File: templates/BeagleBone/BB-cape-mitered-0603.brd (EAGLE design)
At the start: 86.4 x 54.6 mm, 14 parts, among them IC8 EEPROM-I2CSMD

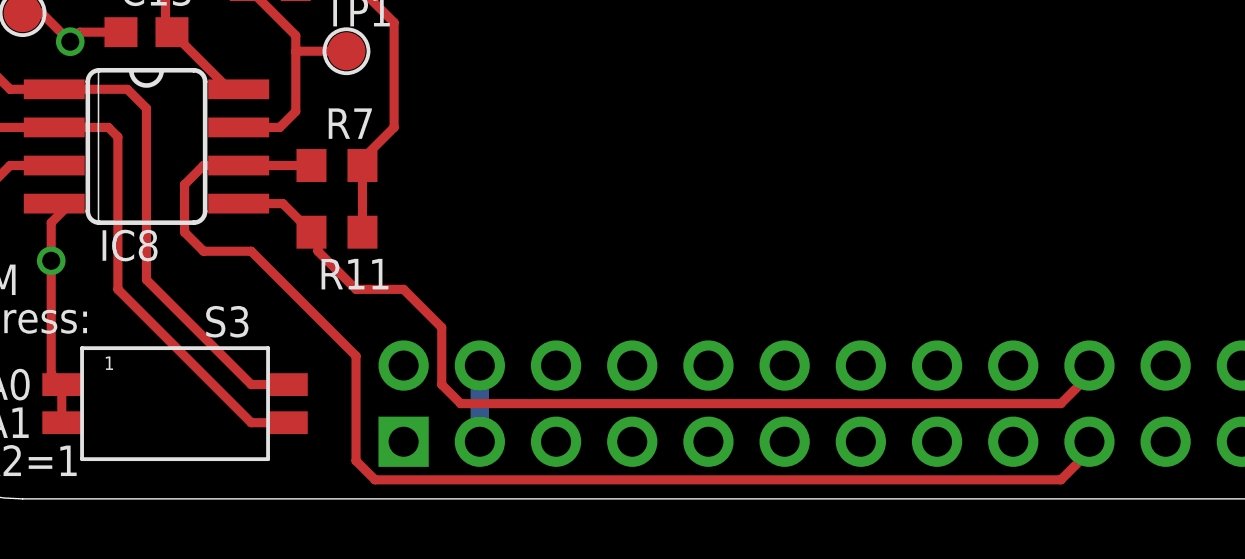
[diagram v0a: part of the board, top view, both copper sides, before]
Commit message: routed power to EEPROM
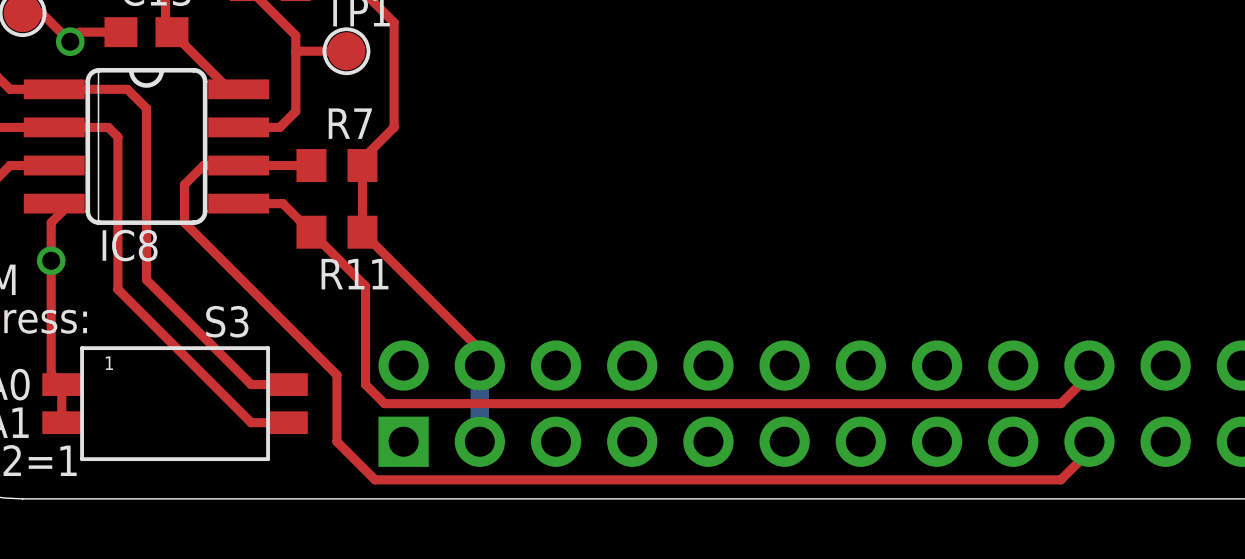
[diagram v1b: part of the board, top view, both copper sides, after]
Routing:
- net 3.3V: track 39.6 -> 45.6 mm
- net I2C2_SCL: track 42.4 -> 41.5 mm
- net I2C2_SDA: track 33.4 -> 34.0 mm
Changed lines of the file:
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@@
 <?xml version="1.0" encoding="utf-8"?>
 <!DOCTYPE eagle SYSTEM "eagle.dtd">
-<eagle version="6.3">
+<eagle version="6.4">
 <drawing>
 <settings>
@@
 <wire x1="13.5509" y1="13.6525" x2="13.2325" y2="13.6525" width="0.3048" layer="1"/>
 <wire x1="13.2325" y1="13.6525" x2="11.3275" y2="15.5575" width="0.3048" layer="1"/>
-<wire x1="17.6775" y1="8.89" x2="21.59" y2="4.445" width="0" layer="19" extent="1-1"/>
+<wire x1="21.59" y1="4.445" x2="21.59" y2="4.9775" width="0.3048" layer="1"/>
+<wire x1="21.59" y1="4.9775" x2="17.6775" y2="8.89" width="0.3048" layer="1"/>
 </signal>
 <signal name="GND">
@@
 <wire x1="15.025" y1="9.8425" x2="15.9775" y2="8.89" width="0.3048" layer="1"/>
 <wire x1="41.91" y1="4.1275" x2="40.9575" y2="3.175" width="0.3048" layer="1"/>
-<wire x1="40.9575" y1="3.175" x2="20.955" y2="3.175" width="0.3048" layer="1"/>
+<wire x1="40.9575" y1="3.175" x2="18.415" y2="3.175" width="0.3048" layer="1"/>
 <wire x1="15.875" y1="9.105" x2="15.9775" y2="8.89" width="0.3048" layer="1"/>
 <contactref element="BB1" pad="P9.20"/>
 <wire x1="41.91" y1="4.1275" x2="41.91" y2="4.445" width="0.3048" layer="1"/>
-<wire x1="20.955" y1="3.175" x2="20.32" y2="3.81" width="0.3048" layer="1"/>
-<wire x1="20.32" y1="3.81" x2="20.32" y2="5.715" width="0.3048" layer="1"/>
-<wire x1="16.1925" y1="8.255" x2="16.1925" y2="8.675" width="0.3048" layer="1"/>
-<wire x1="16.1925" y1="8.675" x2="15.9775" y2="8.89" width="0.3048" layer="1"/>
-<wire x1="20.32" y1="5.715" x2="19.05" y2="6.985" width="0.3048" layer="1"/>
-<wire x1="19.05" y1="6.985" x2="17.4625" y2="6.985" width="0.3048" layer="1"/>
-<wire x1="17.4625" y1="6.985" x2="16.1925" y2="8.255" width="0.3048" layer="1"/>
+<wire x1="18.415" y1="3.175" x2="17.78" y2="3.81" width="0.3048" layer="1"/>
+<wire x1="17.78" y1="3.81" x2="17.78" y2="7.0875" width="0.3048" layer="1"/>
+<wire x1="17.78" y1="7.0875" x2="15.9775" y2="8.89" width="0.3048" layer="1"/>
 </signal>
 <signal name="I2C2_SCL">
@@
 <contactref element="BB1" pad="P9.19"/>
 <wire x1="41.91" y1="1.905" x2="41.91" y2="1.5875" width="0.3048" layer="1"/>
-<wire x1="18.0975" y1="0.635" x2="17.4625" y2="1.27" width="0.3048" layer="1"/>
-<wire x1="11.7475" y1="10.4775" x2="11.7475" y2="8.89" width="0.3048" layer="1"/>
-<wire x1="17.4625" y1="1.27" x2="17.4625" y2="4.7625" width="0.3048" layer="1"/>
-<wire x1="17.4625" y1="4.7625" x2="13.97" y2="8.255" width="0.3048" layer="1"/>
-<wire x1="13.97" y1="8.255" x2="12.3825" y2="8.255" width="0.3048" layer="1"/>
-<wire x1="12.3825" y1="8.255" x2="11.7475" y2="8.89" width="0.3048" layer="1"/>
+<wire x1="18.0975" y1="0.635" x2="16.8275" y2="1.905" width="0.3048" layer="1"/>
+<wire x1="11.7475" y1="10.4775" x2="11.7475" y2="9.2075" width="0.3048" layer="1"/>
+<wire x1="16.8275" y1="1.905" x2="16.8275" y2="4.1275" width="0.3048" layer="1"/>
+<wire x1="16.8275" y1="4.1275" x2="11.7475" y2="9.2075" width="0.3048" layer="1"/>
 </signal>
 <signal name="WP">

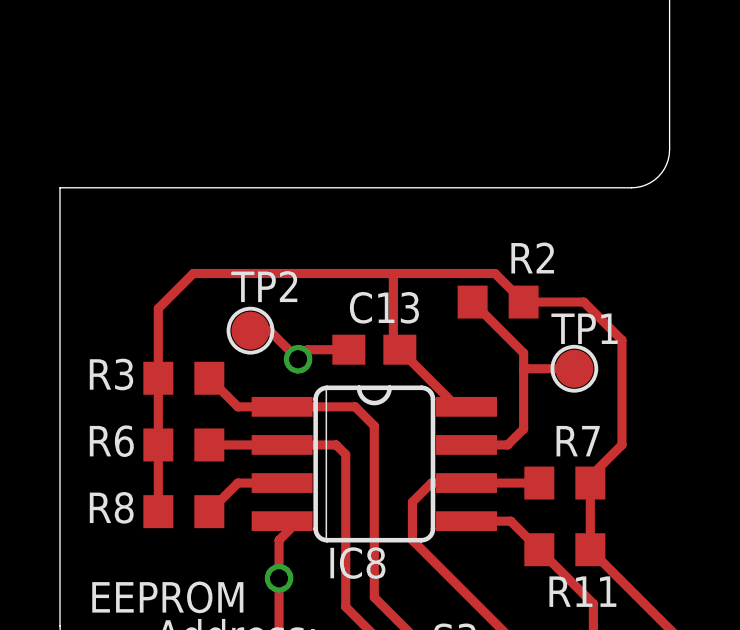
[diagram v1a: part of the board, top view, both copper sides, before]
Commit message: adjusted test point positions to match serial cape
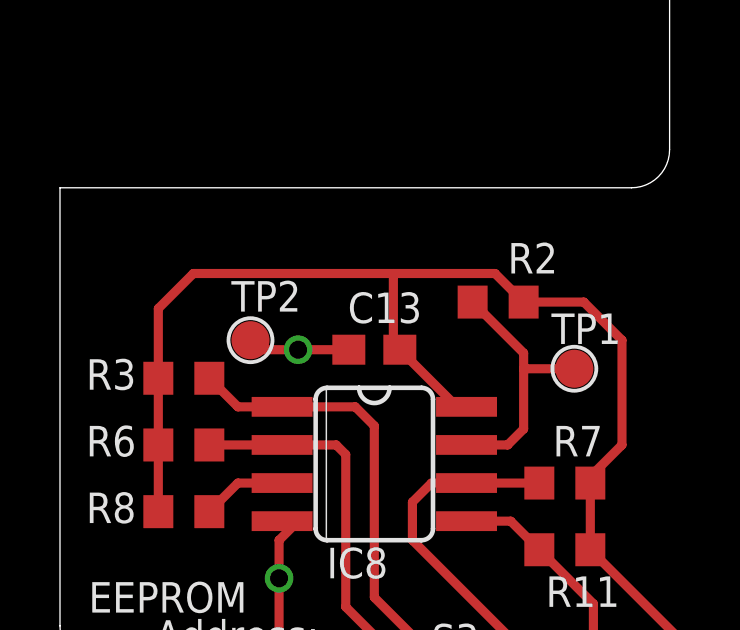
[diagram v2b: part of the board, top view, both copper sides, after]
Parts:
- moved TP2 0.32 mm to (6.35, 15.9)
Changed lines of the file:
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@@
 <element name="BB1" library="logic-supply" package="BB_CAPE_TOP" value="BBH2" x="0" y="0" rot="MR90"/>
 <element name="U$7" library="logic-supply" package="OSHW-LOGO-M" value="OSHW-LOGOM" x="63.8175" y="31.75"/>
-<element name="TP2" library="logic-supply" package="TEST_POINT" value="TEST_POINT" x="6.35" y="16.1925" smashed="yes">
-<attribute name="BOM" value="EXCLUDE" x="6.35" y="16.1925" size="1.778" layer="27" display="off"/>
-<attribute name="DATABASE" value="./../BOM/logic-supply-db.txt" x="6.35" y="16.1925" size="1.778" layer="27" display="off"/>
-<attribute name="NAME" x="5.715" y="17.145" size="1.016" layer="25" font="vector"/>
-<attribute name="VALUE" x="3.81" y="13.6525" size="1.27" layer="27"/>
+<element name="TP2" library="logic-supply" package="TEST_POINT" value="TEST_POINT" x="6.35" y="15.875" smashed="yes">
+<attribute name="BOM" value="EXCLUDE" x="6.35" y="15.875" size="1.778" layer="27" display="off"/>
+<attribute name="DATABASE" value="./../BOM/logic-supply-db.txt" x="6.35" y="15.875" size="1.778" layer="27" display="off"/>
+<attribute name="NAME" x="5.715" y="16.8275" size="1.016" layer="25" font="vector"/>
+<attribute name="VALUE" x="3.81" y="13.335" size="1.27" layer="27"/>
 </element>
 </elements>
@@
 <wire x1="7.3025" y1="9.2075" x2="7.3025" y2="7.9375" width="0.3048" layer="1"/>
 <via x="7.3025" y="7.9375" extent="1-16" drill="0.6"/>
-<wire x1="9.6275" y1="15.5575" x2="8.255" y2="15.5575" width="0.3048" layer="1"/>
-<wire x1="8.255" y1="15.5575" x2="7.9375" y2="15.24" width="0.3048" layer="1"/>
-<via x="7.9375" y="15.24" extent="1-16" drill="0.6"/>
+<wire x1="9.6275" y1="15.5575" x2="7.9375" y2="15.5575" width="0.3048" layer="1"/>
+<via x="7.9375" y="15.5575" extent="1-16" drill="0.6"/>
 <contactref element="BB1" pad="P8.1"/>
 <contactref element="BB1" pad="P8.2"/>
@@
 <wire x1="7.3025" y1="4.1625" x2="7.655" y2="3.81" width="0.3048" layer="1"/>
 <contactref element="TP2" pad="P$1"/>
-<wire x1="6.35" y1="16.1925" x2="6.985" y2="16.1925" width="0.3048" layer="1"/>
-<wire x1="6.985" y1="16.1925" x2="7.9375" y2="15.24" width="0.3048" layer="1"/>
+<wire x1="7.9375" y1="15.5575" x2="6.6675" y2="15.5575" width="0.3048" layer="1"/>
+<wire x1="6.6675" y1="15.5575" x2="6.35" y2="15.875" width="0.3048" layer="1"/>
 <wire x1="74.93" y1="1.905" x2="74.93" y2="4.445" width="0" layer="19" extent="1-1"/>
 <wire x1="72.39" y1="4.445" x2="74.93" y2="4.445" width="0" layer="19" extent="1-1"/>
@@
 <wire x1="19.05" y1="1.905" x2="19.05" y2="4.445" width="0" layer="19" extent="1-1"/>
 <wire x1="7.655" y1="3.81" x2="19.05" y2="4.445" width="0" layer="19" extent="1-1"/>
-<wire x1="7.9375" y1="15.24" x2="7.4041" y2="9.8425" width="0" layer="19" extent="1-1"/>
+<wire x1="7.9375" y1="15.5575" x2="7.4041" y2="9.8425" width="0" layer="19" extent="1-1"/>
 <wire x1="19.05" y1="50.165" x2="9.6275" y2="15.5575" width="0" layer="19" extent="1-1"/>
 <wire x1="19.05" y1="52.705" x2="19.05" y2="50.165" width="0" layer="19" extent="1-1"/>

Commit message: changed pull-ups to srm recommended 5.6k
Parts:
- R11, R2, R3, R6, R7, R8: value 4.7k -> 5.6k
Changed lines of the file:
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@@
 </element>
 <element name="U$4" library="logic-supply" package="LOGO-LGX-LARGE" value="LOGO-LGX_LARGE" x="41.5925" y="31.75" smashed="yes"/>
-<element name="R7" library="rcl" package="R0603" value="4.7k" x="16.8275" y="11.1125" smashed="yes">
+<element name="R7" library="rcl" package="R0603" value="5.6k" x="16.8275" y="11.1125" smashed="yes">
 <attribute name="NAME" x="18.0975" y="13.0175" size="1.016" layer="25" font="vector" rot="R180"/>
 <attribute name="VALUE" x="16.1925" y="9.2075" size="1.27" layer="27"/>
 <attribute name="PARTNO" value="RC0603FR-074K7L" x="16.8275" y="11.1125" size="1.778" layer="27" display="off"/>
 </element>
-<element name="R11" library="rcl" package="R0603" value="4.7k" x="16.8275" y="8.89" smashed="yes">
+<element name="R11" library="rcl" package="R0603" value="5.6k" x="16.8275" y="8.89" smashed="yes">
 <attribute name="NAME" x="16.1925" y="6.985" size="1.016" layer="25" font="vector"/>
 <attribute name="VALUE" x="16.1925" y="6.985" size="1.27" layer="27"/>
 <attribute name="PARTNO" value="RC0603FR-074K7L" x="16.8275" y="8.89" size="1.778" layer="27" display="off"/>
 </element>
-<element name="R2" library="rcl" package="R0603" value="4.7k" x="14.605" y="17.145" smashed="yes">
+<element name="R2" library="rcl" package="R0603" value="5.6k" x="14.605" y="17.145" smashed="yes">
 <attribute name="NAME" x="14.9225" y="18.0975" size="1.016" layer="25" font="vector"/>
 <attribute name="VALUE" x="13.97" y="15.24" size="1.27" layer="27"/>
@@
 <attribute name="BOM" value="EXCLUDE" x="17.145" y="14.9225" size="1.778" layer="27" display="off"/>
 </element>
-<element name="R3" library="rcl" package="R0603" value="4.7k" x="4.1275" y="14.605" smashed="yes" rot="R180">
+<element name="R3" library="rcl" package="R0603" value="5.6k" x="4.1275" y="14.605" smashed="yes" rot="R180">
 <attribute name="NAME" x="2.54" y="15.24" size="1.016" layer="25" font="vector" rot="R180"/>
 <attribute name="VALUE" x="4.7625" y="16.51" size="1.27" layer="27" rot="R180"/>
 <attribute name="PARTNO" value="RC0603FR-074K7L" x="4.1275" y="14.605" size="1.778" layer="27" rot="R180" display="off"/>
 </element>
-<element name="R6" library="rcl" package="R0603" value="4.7k" x="4.1275" y="12.3825" smashed="yes" rot="R180">
+<element name="R6" library="rcl" package="R0603" value="5.6k" x="4.1275" y="12.3825" smashed="yes" rot="R180">
 <attribute name="NAME" x="2.54" y="13.0175" size="1.016" layer="25" font="vector" rot="R180"/>
 <attribute name="VALUE" x="4.7625" y="14.2875" size="1.27" layer="27" rot="R180"/>
 <attribute name="PARTNO" value="RC0603FR-074K7L" x="4.1275" y="12.3825" size="1.778" layer="27" rot="R180" display="off"/>
 </element>
-<element name="R8" library="rcl" package="R0603" value="4.7k" x="4.1275" y="10.16" smashed="yes" rot="R180">
+<element name="R8" library="rcl" package="R0603" value="5.6k" x="4.1275" y="10.16" smashed="yes" rot="R180">
 <attribute name="NAME" x="2.54" y="10.795" size="1.016" layer="25" font="vector" rot="R180"/>
 <attribute name="VALUE" x="4.7625" y="12.065" size="1.27" layer="27" rot="R180"/>

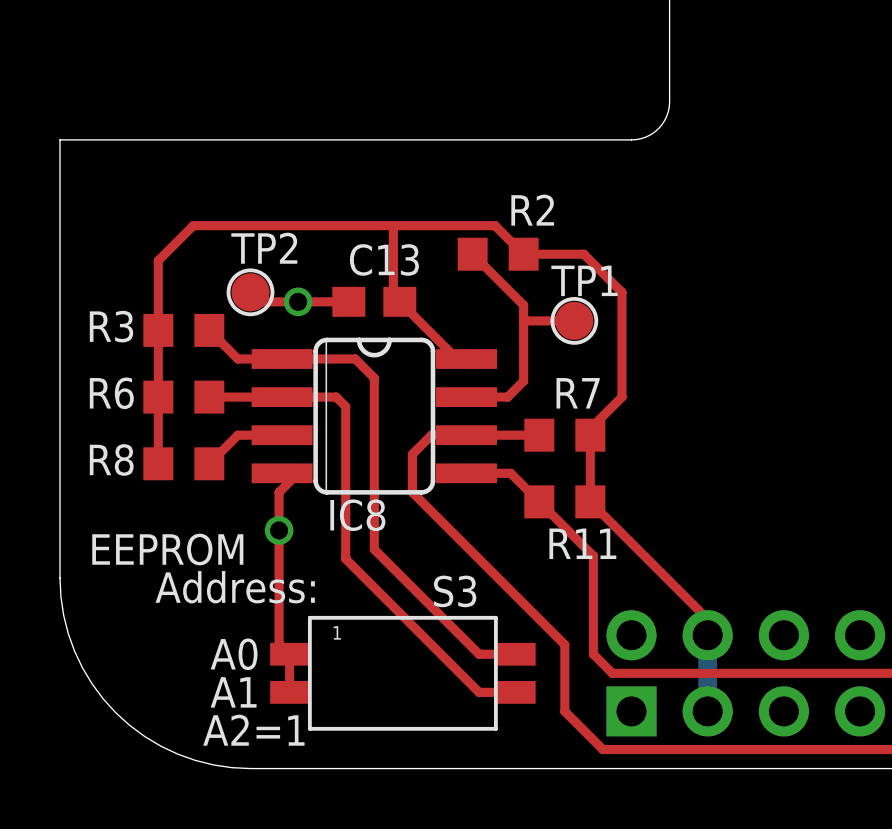
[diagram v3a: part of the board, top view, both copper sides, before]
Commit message: consolidated EEPROM layout (moved test points)
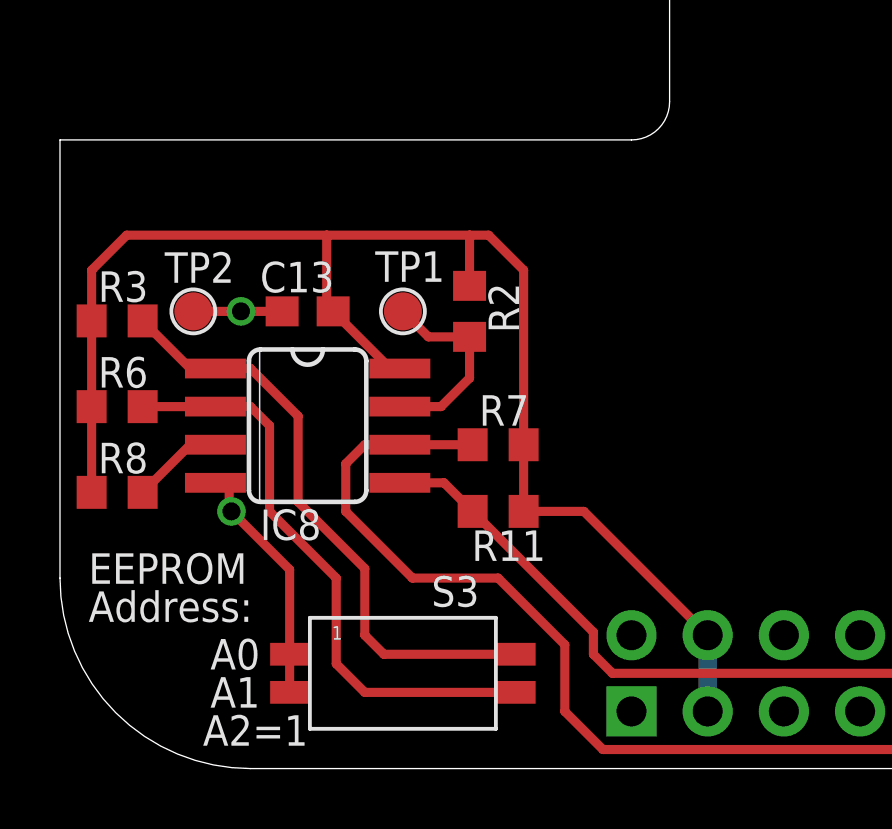
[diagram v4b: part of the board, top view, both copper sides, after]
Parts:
- moved TP1 5.72 mm to (11.4, 15.2)
- moved R8 2.42 mm to (1.91, 9.21)
- moved R11 2.25 mm to (14.6, 8.57)
- moved R6 2.25 mm to (1.91, 12.1)
- moved R7 2.25 mm to (14.6, 10.8)
- moved R3 2.25 mm to (1.91, 14.9)
- moved IC8 2.25 mm to (8.26, 11.4)
- moved C13 2.25 mm to (8.26, 15.2)
- moved R2 2.13 mm to (13.7, 15.2), turned to 90 degrees
- moved TP2 2.01 mm to (4.45, 15.2)
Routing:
- net 3.3V: track 45.6 -> 48.9 mm
- net N$14: track 17.3 -> 19.7 mm
- net I2C2_SCL: track 41.5 -> 43.8 mm
- net WP: track 8.75 -> 6.67 mm
- net N$13: track 18.0 -> 20.0 mm
- net I2C2_SDA: track 34.0 -> 34.6 mm
